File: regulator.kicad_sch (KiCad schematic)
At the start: 4 parts

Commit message: Added rdac sheet
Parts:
- added EA1: Engine_Alternator, symbol gary aircraft symbol library:Engine_Alternator
- added F1, F2: Fuse, symbol Device:Fuse
- added PL15 (x3), PL15/9: Conn_01x01, symbol Connector_Generic:Conn_01x01
- added S?: Starter_Solenoid, symbol gary aircraft symbol library:Starter_Solenoid
- added S?: Isolator_Solenoid, symbol gary aircraft symbol library:Isolator_Solenoid
- added SM1: Starter_Motor, symbol gary aircraft symbol library:Starter_Motor
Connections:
- net Alternator Master CB: now reaches C?.1, TB3. (9B), U?.3 (R), U?.4 (+B), U?.5 (C)
- net Alternator Master CB: now also F2.1
- net GND: now reaches C?.2, TB3. (9B), U?.7 (Ground)
- net GND: now also BT?.2 (-), EA1. (T2), S?. (Start_Engaged), SM1. (Power)
- net at BT?.1 (+): now also S?. (Enable)
- net at TB3. (9B), U?.1 (G1): now also EA1. (T2)
- net at TB3. (9B), U?.2 (G2): now also EA1. (T2)
- new net: F2.2, PL15/9.1 (Pin_1)
- new net: PL15.1 (Pin_1), S?. (Enable)
- new net: S?. (Start_Engaged), SM1. (Power)
- new net: F1.2, PL15.1 (Pin_1)
- new net: F1.1, S?. (Start_Engaged)
- new net: PL15.1 (Pin_1), S?. (Start_Engaged)
- new net Battery Master CB: S?. (Enable), S?. (Start_Engaged)
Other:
- note added: "Ground strap to engine block"
- title: (none) -> Europa - Alternator, Regulator, and Battery
- moved on the sheet: BT?, C?, TB3, U?

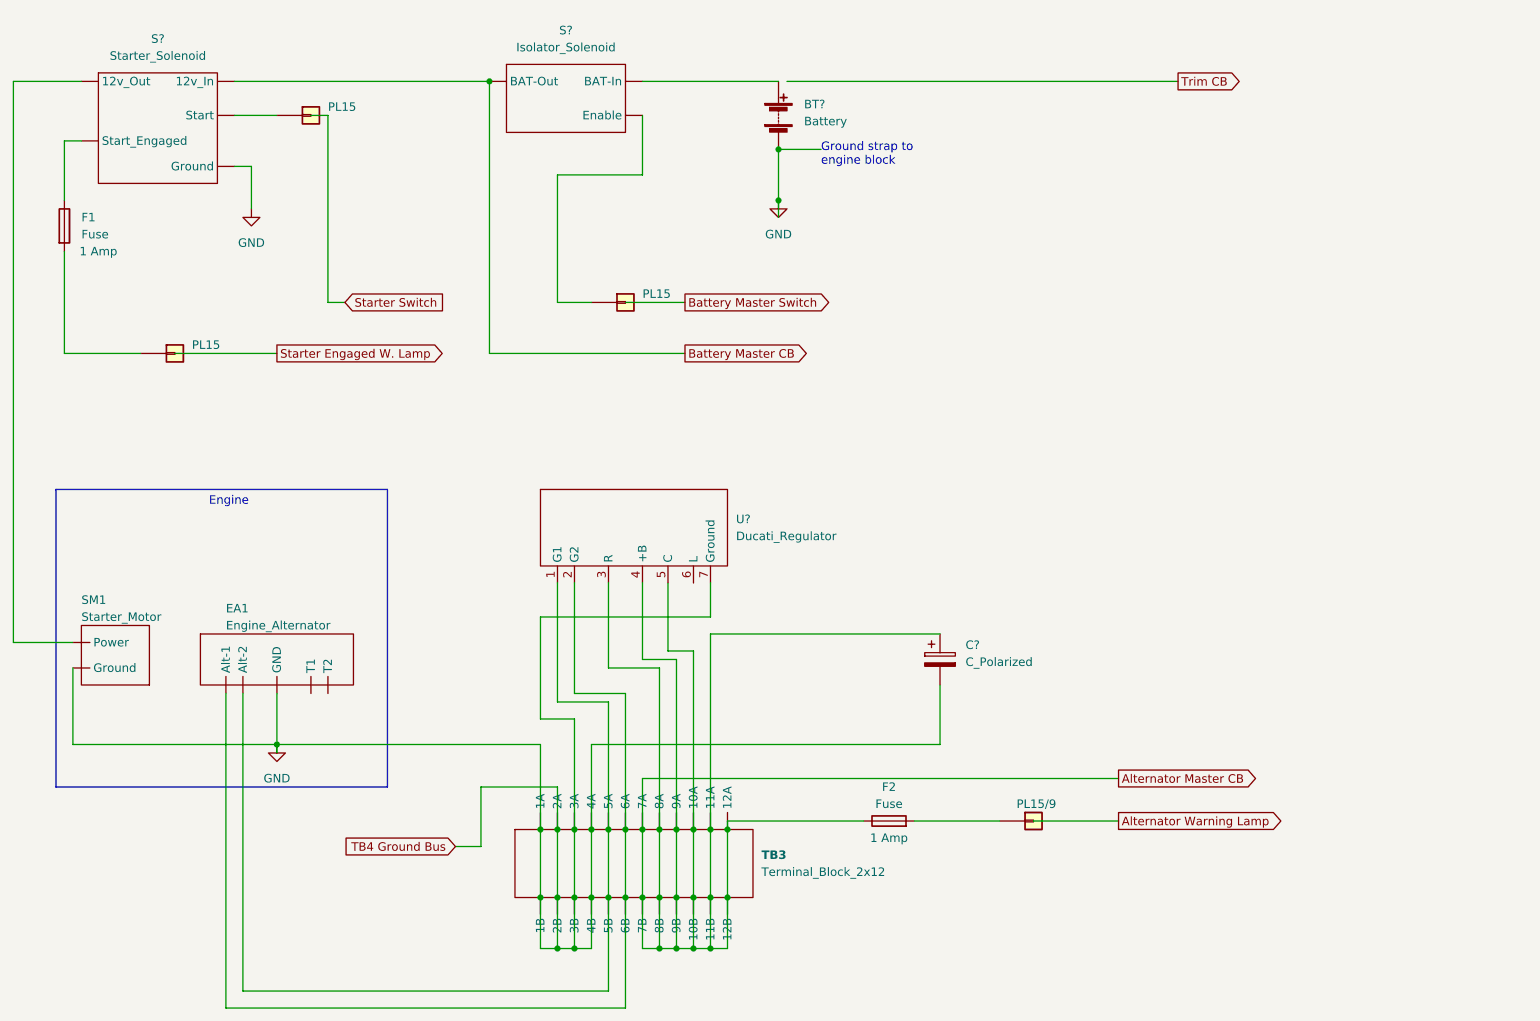
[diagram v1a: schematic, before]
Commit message: Added Main Instrument Panel and Main Bus Panel
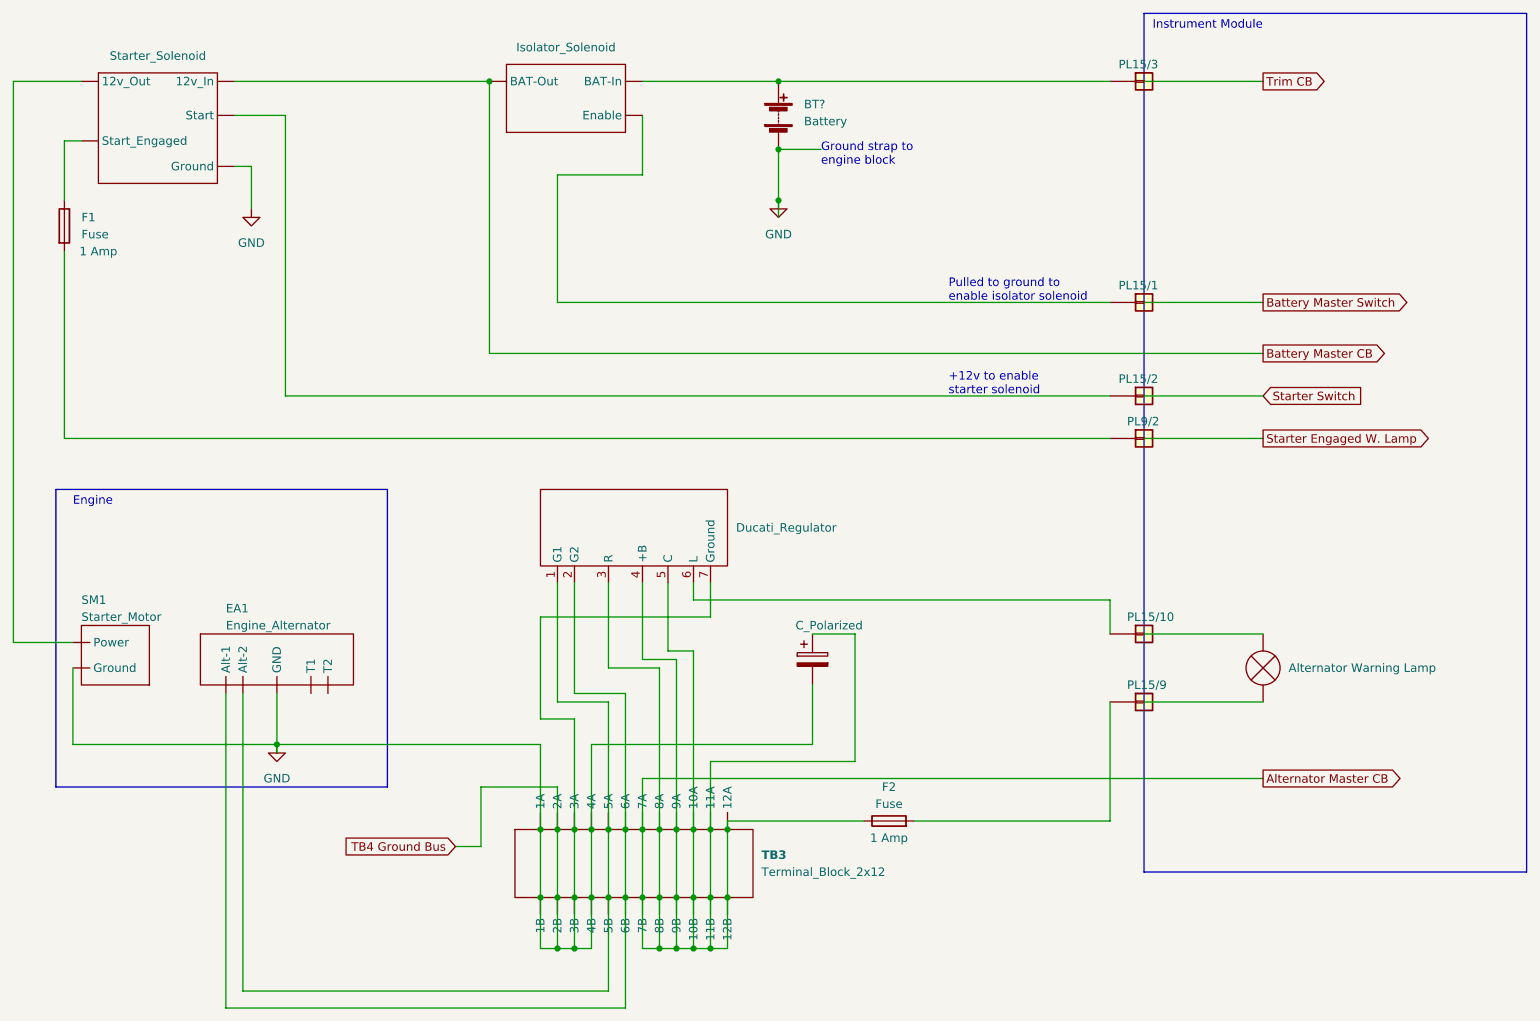
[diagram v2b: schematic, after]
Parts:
- added LA?: Alternator Warning Lamp, symbol Device:Lamp
- added PL15/10, PL15/3: Conn_01x01, symbol Connector_Generic:Conn_01x01
- renumbered PL15 to PL15/1, PL15 to PL15/2, PL15 to PL9/2
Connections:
- net at BT?.1 (+), S?. (Enable): now also PL15/3.1 (Pin_1)
- net at U?.6 (L): now also PL15/10.1 (Pin_1)
- new net: EA1. (T2), TB3. (9B), U?.1 (G1)
- new net: EA1. (T2), TB3. (9B), U?.2 (G2)
- new net: S?. (Start_Engaged), SM1. (Power)
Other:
- note added: "+12v to enable starter solenoid"
- note added: "Instrument Module"
- note added: "Pulled to ground to enable isolator solenoid"
- moved on the sheet: PL15/1, PL15/2, PL15/9, PL9/2

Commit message: Added Trim Circuit and Avionics Bus
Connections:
- new net: EA1. (T2), TB3. (9B), U?.1 (G1)
- new net: EA1. (T2), TB3. (9B), U?.2 (G2)
- new net: S?. (Start_Engaged), SM1. (Power)

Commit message: Proof reading and snagging updates
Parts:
- removed F2: Fuse, symbol Device:Fuse
- added FB1/1: Fuse, symbol Device:Fuse
- FB1/2: renamed from F1; Rating 1 Amp -> 2 Amp
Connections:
- net Alternator Master CB: now also PL15/9.1 (Pin_1)
- new net: EA1. (T2), TB3. (9B), U?.1 (G1)
- new net: EA1. (T2), TB3. (9B), U?.2 (G2)
- new net: BT?.1 (+), FB1/1.1, S?. (Enable)
- new net: S?. (Start_Engaged), SM1. (Power)
- new net: FB1/1.2, PL15/3.1 (Pin_1)
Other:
- note added: "1 - 4 @ 0volt"
- note added: "7 - 12 @ +12volt"
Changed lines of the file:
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@@
   (title_block
     (title "Europa - Alternator, Regulator, and Battery")
-    (date "2022-12-17")
+    (date "2022-12-22")
     (rev "3")
   )
@@
   (junction (at 127 144.78) (diameter 0) (color 0 0 0 0)
   )
+  (junction (at 147.32 33.02) (diameter 0) (color 0 0 0 0)
+  )
   (junction (at 129.54 154.94) (diameter 0) (color 0 0 0 0)
   )
@@
   (junction (at 134.62 144.78) (diameter 0) (color 0 0 0 0)
   )
-  (junction (at 147.32 33.02) (diameter 0) (color 0 0 0 0)
-  )
   (junction (at 72.39 132.08) (diameter 0) (color 0 0 0 0)
   )
@@
     (stroke (width 0) (type default) (color 0 0 0 0))
   )
-  (wire (pts (xy 147.32 33.02) (xy 196.85 33.02))
-    (stroke (width 0) (type default) (color 0 0 0 0))
-  )
   (wire (pts (xy 152.4 132.08) (xy 152.4 123.19))
     (stroke (width 0) (type default) (color 0 0 0 0))
@@
     (stroke (width 0) (type default) (color 0 0 0 0))
   )
+  (wire (pts (xy 147.32 33.02) (xy 168.91 33.02))
+    (stroke (width 0) (type default) (color 0 0 0 0))
+  )
   (polyline (pts (xy 201.93 22.86) (xy 259.08 22.86))
     (stroke (width 0) (type default) (color 0 0 0 0))
@@
     (stroke (width 0) (type default) (color 0 0 0 0))
   )
+  (wire (pts (xy 176.53 33.02) (xy 196.85 33.02))
+    (stroke (width 0) (type default) (color 0 0 0 0))
+  )
   (wire (pts (xy 114.3 138.43) (xy 102.87 138.43))
     (stroke (width 0) (type default) (color 0 0 0 0))
@@
     (stroke (width 0) (type default) (color 0 0 0 0))
   )
-  (wire (pts (xy 139.7 143.51) (xy 160.02 143.51))
-    (stroke (width 0) (type default) (color 0 0 0 0))
-  )
   (wire (pts (xy 201.93 33.02) (xy 219.71 33.02))
     (stroke (width 0) (type default) (color 0 0 0 0))
@@
     (stroke (width 0) (type default) (color 0 0 0 0))
   )
-  (wire (pts (xy 167.64 143.51) (xy 196.85 143.51))
+  (wire (pts (xy 139.7 143.51) (xy 196.85 143.51))
     (stroke (width 0) (type default) (color 0 0 0 0))
   )
@@
     (effects (font (size 1.27 1.27)) (justify left bottom))
   )
+  (text "1 - 4 @ 0volt" (at 105.41 165.1 0)
+    (effects (font (size 1.27 1.27)) (justify left bottom))
+  )
   (text "Pulled to ground to \nenable isolator solenoid" (at 172.72 66.04 0)
     (effects (font (size 1.27 1.27)) (justify left bottom))
@@
   )
   (text "+12v to enable\nstarter solenoid" (at 172.72 80.01 0)
+    (effects (font (size 1.27 1.27)) (justify left bottom))
+  )
+  (text "7 - 12 @ +12volt" (at 127 165.1 0)
     (effects (font (size 1.27 1.27)) (justify left bottom))
   )
@@
     (pin "1")
   )
+  (symbol (lib_id "Device:Fuse") (at 172.72 33.02 90) (unit 1)
+    (in_bom yes) (on_board yes)
+    (property "Reference" "FB1/1" (id 0) (at 172.72 26.67 90))
+    (property "Value" "Fuse" (id 1) (at 172.72 29.21 90))
+    (property "Footprint" "" (id 2) (at 172.72 34.798 90)
+      (effects (font (size 1.27 1.27)) hide)
+    )
+    (property "Datasheet" "~" (id 3) (at 172.72 33.02 0)
+      (effects (font (size 1.27 1.27)) hide)
+    )
+    (property "Rating" "2 Amp" (id 4) (at 172.72 35.56 90))
+    (pin "1")
+    (pin "2")
+  )
   (symbol (lib_id "Device:Fuse") (at 40.64 54.61 0) (unit 1)
     (in_bom yes) (on_board yes)
-    (property "Reference" "F1" (id 0) (at 43.18 53.3399 0)
+    (property "Reference" "FB1/2" (id 0) (at 43.18 53.3399 0)
       (effects (font (size 1.27 1.27)) (justify left))
     )
@@
       (effects (font (size 1.27 1.27)) hide)
     )
-    (property "Rating" "1 Amp" (id 4) (at 45.72 58.42 0))
+    (property "Rating" "2 Amp" (id 4) (at 45.72 58.42 0))
     (pin "1")
     (pin "2")
-  )
-  (symbol (lib_id "Device:Fuse") (at 163.83 143.51 90) (unit 1)
-    (in_bom yes) (on_board yes)
-    (property "Reference" "F2" (id 0) (at 163.83 138.43 90))
-    (property "Value" "Fuse" (id 1) (at 163.83 140.97 90))
-    (property "Footprint" "" (id 2) (at 163.83 145.288 90)
-      (effects (font (size 1.27 1.27)) hide)
-    )
-    (property "Datasheet" "~" (id 3) (at 163.83 143.51 0)
-      (effects (font (size 1.27 1.27)) hide)
-    )
-    (property "Rating" "1 Amp" (id 4) (at 163.83 146.05 90))
-    (pin "1")
-    (pin "2")

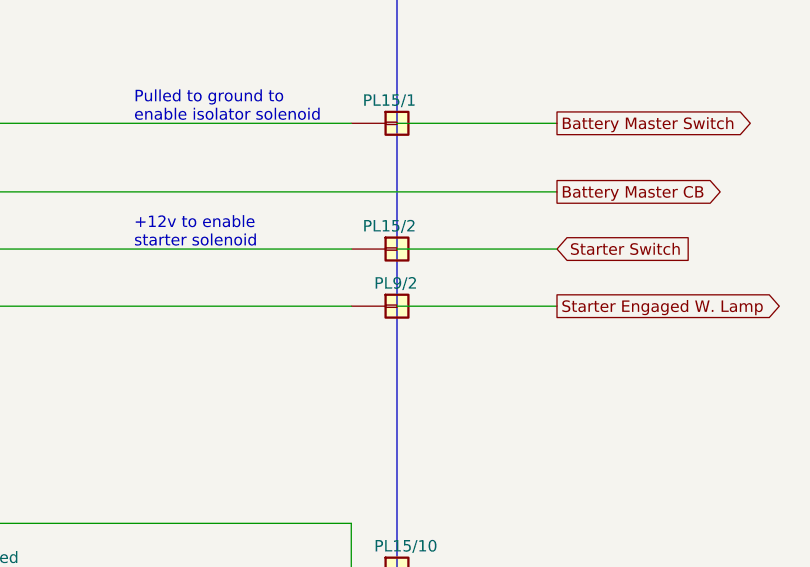
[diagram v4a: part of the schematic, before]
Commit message: Updates from manual validation
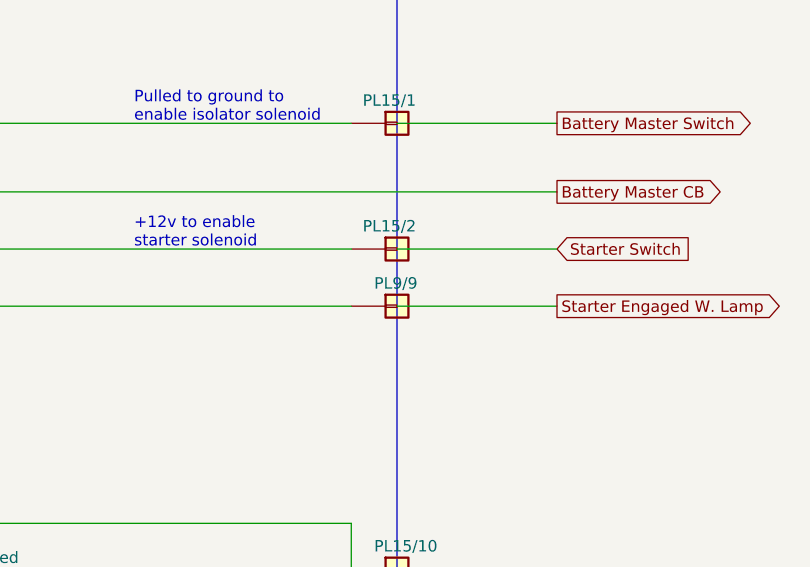
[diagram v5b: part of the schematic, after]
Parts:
- renumbered PL9/2 to PL9/9
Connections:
- new net: EA1. (T2), TB3. (9B), U?.1 (G1)
- new net: EA1. (T2), TB3. (9B), U?.2 (G2)
- new net: S?. (Start_Engaged), SM1. (Power)
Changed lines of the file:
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@@
   (title_block
     (title "Europa - Alternator, Regulator, and Battery")
-    (date "2022-12-22")
-    (rev "3")
+    (date "2022-12-24")
+    (rev "4")
   )
   (junction (at 127 154.94) (diameter 0) (color 0 0 0 0)
@@
   (symbol (lib_id "Connector_Generic:Conn_01x01") (at 201.93 86.36 0) (unit 1)
     (in_bom yes) (on_board no)
-    (property "Reference" "PL9/2" (id 0) (at 199.39 83.82 0)
-      (effects (font (size 1.27 1.27)) (justify left))
-    )
+    (property "Reference" "PL9/9" (id 0) (at 199.39 83.82 0)
+      (effects (font (size 1.27 1.27)) (justify left))
+    )

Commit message: Small updates to multiple sheets, and major update to SmartAss sheet
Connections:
- new net: EA1. (T2), TB3. (9B), U?.1 (G1)
- new net: EA1. (T2), TB3. (9B), U?.2 (G2)
- new net: S?. (Start_Engaged), SM1. (Power)

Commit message: Added Fuel Flow Sensor
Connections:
- new net: EA1. (T2), TB3. (9B), U?.1 (G1)
- new net: EA1. (T2), TB3. (9B), U?.2 (G2)
- new net: S?. (Start_Engaged), SM1. (Power)

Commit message: Added PL20 to COM Sheet
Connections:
- new net: EA1. (T2), TB3. (9B), U?.1 (G1)
- new net: EA1. (T2), TB3. (9B), U?.2 (G2)
- new net: S?. (Start_Engaged), SM1. (Power)
